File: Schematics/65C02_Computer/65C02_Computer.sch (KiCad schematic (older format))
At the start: 1 part

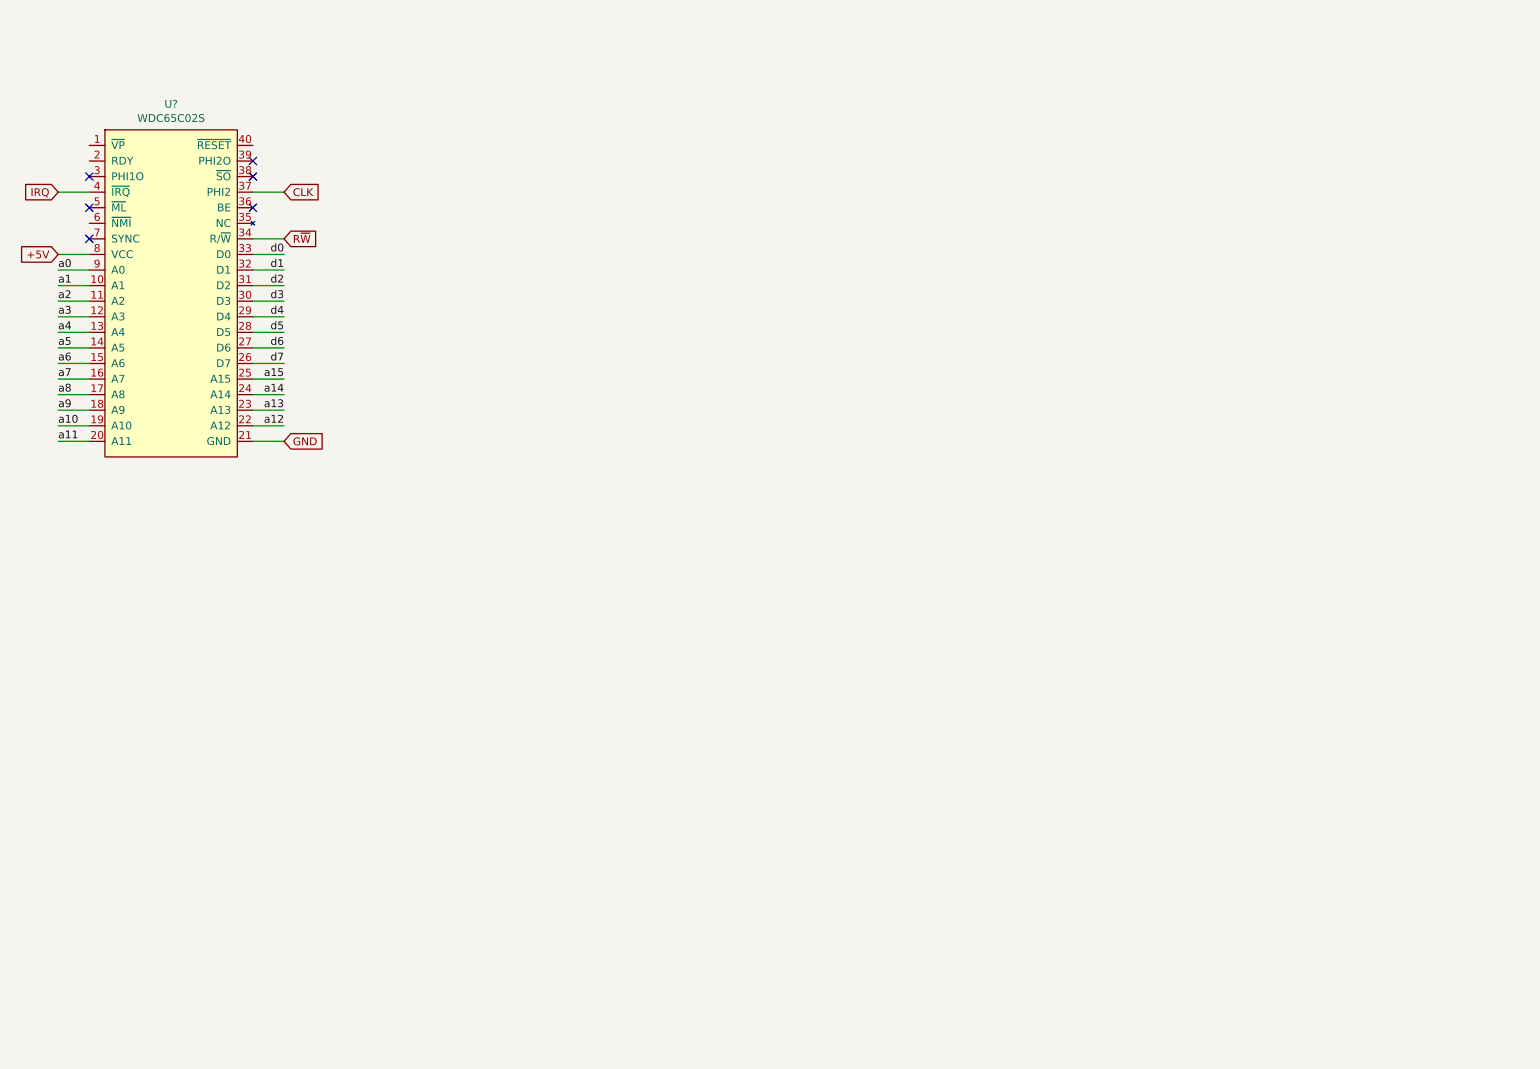
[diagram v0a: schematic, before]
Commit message: Added VIA chips to schematic
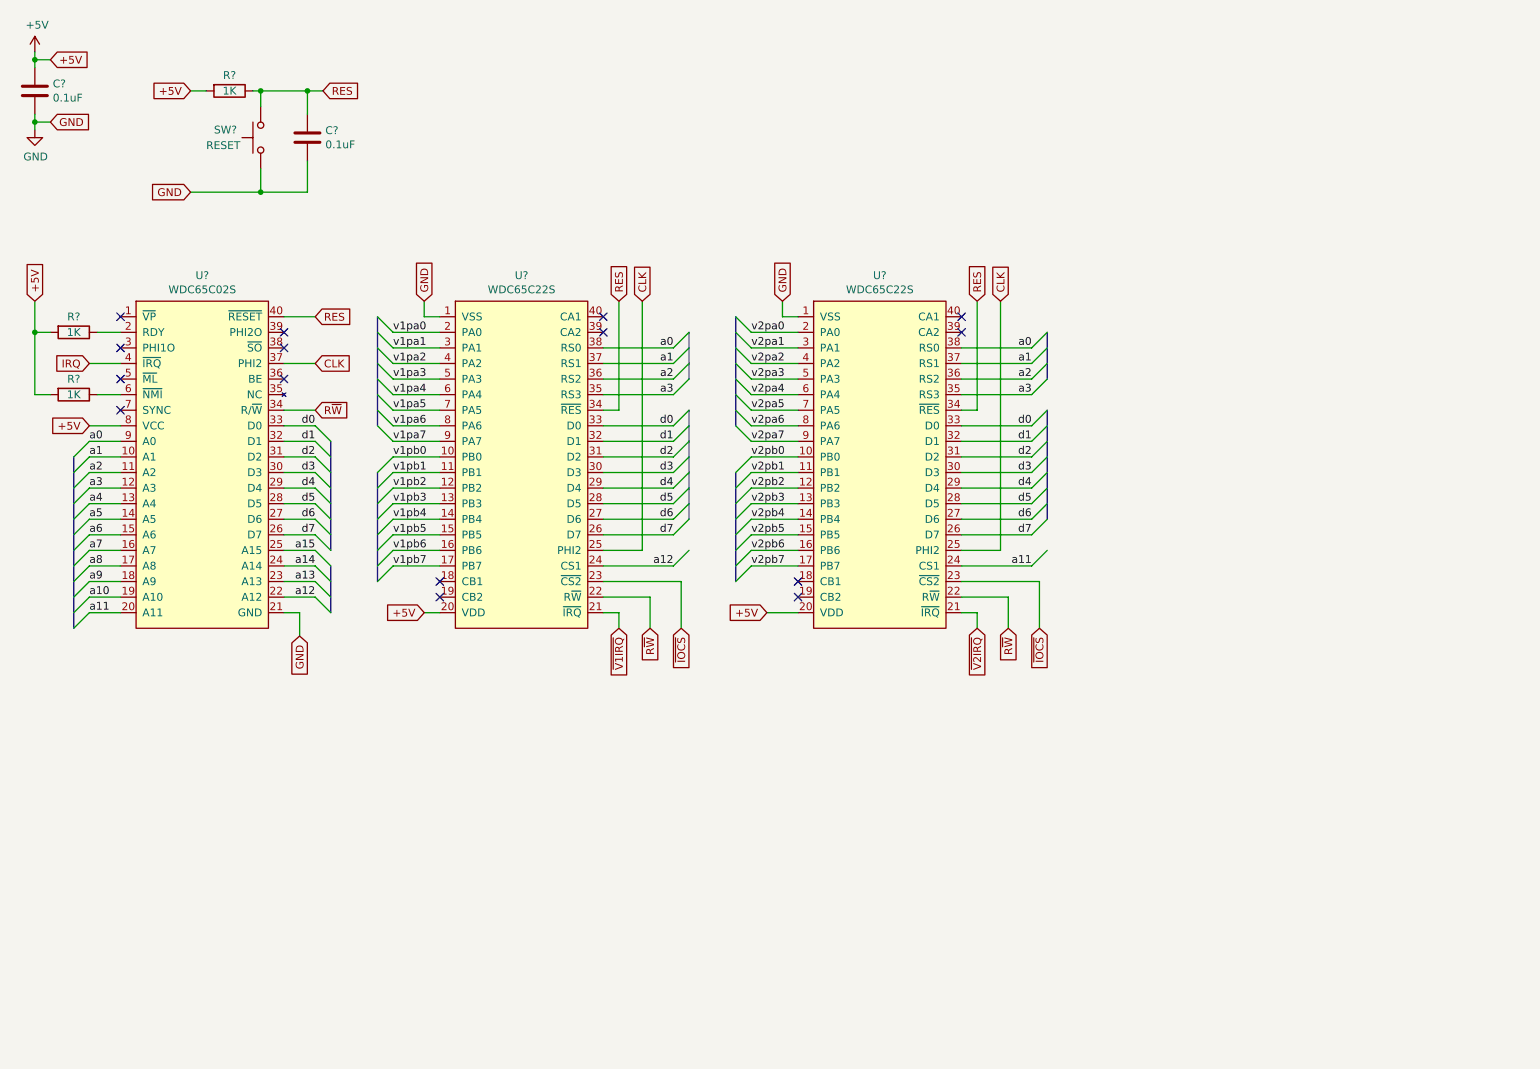
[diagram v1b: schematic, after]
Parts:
- added C? (x2): 0.1uF, symbol Device:C
- added R? (x3): 1K, symbol Device:R
- added SW?: RESET, symbol Switch:SW_Push
- added U? (x2): WDC65C22S, Package_DIP:DIP-40_W15.24mm_Socket, symbol 6502:WDC65C22S
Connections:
- net +5V: now also C?.1, R?.2, R?.2, R?.2, U?.20 (VDD), U?.20 (VDD)
- net CLK: now also U?.25 (PHI2), U?.25 (PHI2)
- net GND: now also C?.2, C?.2, SW?.1, U?.1 (VSS), U?.1 (VSS)
- net R~W: now also U?.22 (R~W), U?.22 (R~W)
- net a0: now also U?.38 (RS0), U?.38 (RS0)
- net a1: now also U?.37 (RS1), U?.37 (RS1)
- net a11: now also U?.24 (CS1)
- net a12: now also U?.24 (CS1)
- net a2: now also U?.36 (RS2), U?.36 (RS2)
- net a3: now also U?.35 (RS3), U?.35 (RS3)
- net d0: now also U?.33 (D0), U?.33 (D0)
- net d1: now also U?.32 (D1), U?.32 (D1)
- net d2: now also U?.31 (D2), U?.31 (D2)
- net d3: now also U?.30 (D3), U?.30 (D3)
- net d4: now also U?.29 (D4), U?.29 (D4)
- net d5: now also U?.28 (D5), U?.28 (D5)
- net d6: now also U?.27 (D6), U?.27 (D6)
- net d7: now also U?.26 (D7), U?.26 (D7)
- net at U?.2 (RDY): now also R?.1
- net RES: now reaches U?.40 (~RESET)
- net RES: now also C?.1, R?.1, SW?.2, U?.34 (~RES), U?.34 (~RES)
- net at U?.6 (~NMI): now also R?.1
- new net v1pa0: U?.2 (PA0)
- new net v1pa1: U?.3 (PA1)
- new net v1pa2: U?.4 (PA2)
- new net v1pa3: U?.5 (PA3)
- new net v1pa4: U?.6 (PA4)
- new net v1pa5: U?.7 (PA5)
- new net v1pa6: U?.8 (PA6)
- new net v1pa7: U?.9 (PA7)
- new net v1pb0: U?.10 (PB0)
- new net v1pb1: U?.11 (PB1)
- new net v1pb2: U?.12 (PB2)
- new net v1pb3: U?.13 (PB3)
- new net v1pb4: U?.14 (PB4)
- new net v1pb5: U?.15 (PB5)
- new net v1pb6: U?.16 (PB6)
- new net v1pb7: U?.17 (PB7)
- new net v2pa0: U?.2 (PA0)
- new net v2pa1: U?.3 (PA1)
- new net v2pa2: U?.4 (PA2)
- new net v2pa3: U?.5 (PA3)
- new net v2pa4: U?.6 (PA4)
- new net v2pa5: U?.7 (PA5)
- new net v2pa6: U?.8 (PA6)
- new net v2pa7: U?.9 (PA7)
- new net v2pb0: U?.10 (PB0)
- new net v2pb1: U?.11 (PB1)
- new net v2pb2: U?.12 (PB2)
- new net v2pb3: U?.13 (PB3)
- new net v2pb4: U?.14 (PB4)
- new net v2pb5: U?.15 (PB5)
- new net v2pb6: U?.16 (PB6)
- new net v2pb7: U?.17 (PB7)
- new net ~IOCS: U?.23 (~CS2), U?.23 (~CS2)
- new net ~V1IRQ: U?.21 (~IRQ)
- new net ~V2IRQ: U?.21 (~IRQ)
- no-connect marks 6 -> 15
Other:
- moved on the sheet: U?

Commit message: Added two oscillators
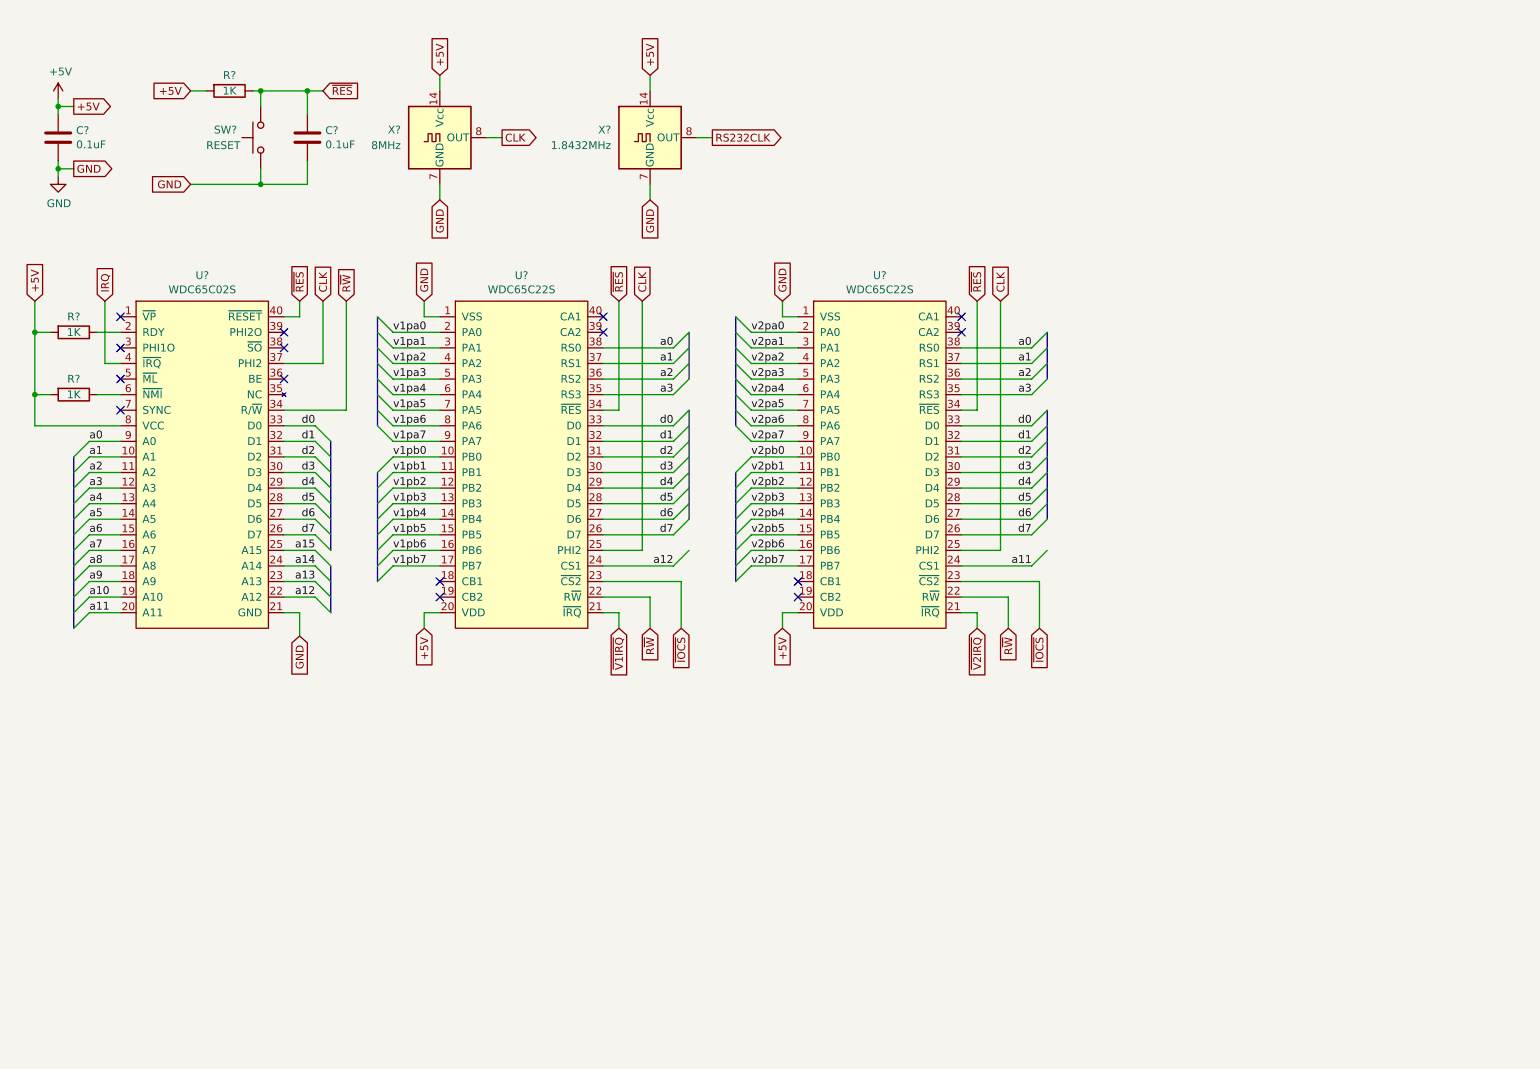
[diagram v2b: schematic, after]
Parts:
- added X?: 8MHz, Oscillator:Oscillator_DIP-14, symbol Oscillator:ACO-xxxMHz
- added X?: 1.8432MHz, Oscillator:Oscillator_DIP-14, symbol Oscillator:ACO-xxxMHz
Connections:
- net +5V: now also X?.14 (Vcc), X?.14 (Vcc)
- net CLK: now also X?.8 (OUT)
- net GND: now also X?.7 (GND), X?.7 (GND)
- net RES renamed ~RES
- new net RS232CLK: X?.8 (OUT)
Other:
- moved on the sheet: C?
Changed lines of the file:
@@
 encoding utf-8
 Sheet 1 1
-Title ""
-Date ""
-Rev ""
+Title "65C02 Hobby Computer"
+Date "2020-01-07"
+Rev "v001"
 Comp ""
 Comment1 ""
 Comment2 ""
-Comment3 ""
-Comment4 ""
+Comment3 "Based on Ben Eater's design"
+Comment4 "Author: Dawid Buchwald"
 $EndDescr
 $Comp
@@
 	1    0    0    -1
 $EndComp
-Text GLabel 1500 2900 0    50   Input ~ 0
+Text GLabel 1600 2500 1    50   Input ~ 0
 IRQ
 Wire Wire Line
-	1500 2900 1700 2900
-Text GLabel 2950 2900 2    50   Input ~ 0
+	1600 2500 1600 2900
+Text GLabel 3000 2500 1    50   Input ~ 0
 CLK
 Wire Wire Line
-	2950 2900 2750 2900
+	3000 2900 2750 2900
 Text GLabel 2850 4650 3    50   Input ~ 0
 GND
-Text GLabel 1500 3300 0    50   Input ~ 0
-+5V
-Wire Wire Line
-	1500 3300 1700 3300
 Text Label 1500 3400 0    50   ~ 0
 a0
@@
 Wire Wire Line
 	2750 3300 2950 3300
-Text GLabel 2950 3200 2    50   Input ~ 0
+Text GLabel 3150 2500 1    50   Input ~ 0
 R~W
 Wire Wire Line
-	2950 3200 2750 3200
+	3150 3200 2750 3200
 NoConn ~ 2750 3000
 NoConn ~ 2750 2800
@@
 Text GLabel 1150 2500 1    50   Input ~ 0
 +5V
-Text GLabel 2950 2600 2    50   Input ~ 0
-RES
-Wire Wire Line
-	2950 2600 2750 2600
+Text GLabel 2850 2500 1    50   Input ~ 0
+~RES
+Wire Wire Line
+	2850 2600 2750 2600
 Wire Wire Line
 	2750 4500 2850 4500
@@
 L power:+5V #PWR?
 U 1 1 5E15AAC6
-P 1150 900
-F 0 "#PWR?" H 1150 750 50  0001 C CNN
-F 1 "+5V" H 1165 1073 50  0000 C CNN
-F 2 "" H 1150 900 50  0001 C CNN
-F 3 "" H 1150 900 50  0001 C CNN
-	1    1150 900
+P 1300 1200
+F 0 "#PWR?" H 1300 1050 50  0001 C CNN
+F 1 "+5V" H 1315 1373 50  0000 C CNN
+F 2 "" H 1300 1200 50  0001 C CNN
+F 3 "" H 1300 1200 50  0001 C CNN
+	1    1300 1200
 	1    0    0    -1
 $EndComp
@@
 L power:GND #PWR?
 U 1 1 5E15AF3A
-P 1150 1400
-F 0 "#PWR?" H 1150 1150 50  0001 C CNN
-F 1 "GND" H 1155 1227 50  0000 C CNN
-F 2 "" H 1150 1400 50  0001 C CNN
-F 3 "" H 1150 1400 50  0001 C CNN
-	1    1150 1400
+P 1300 1700
+F 0 "#PWR?" H 1300 1450 50  0001 C CNN
+F 1 "GND" H 1305 1527 50  0000 C CNN
+F 2 "" H 1300 1700 50  0001 C CNN
+F 3 "" H 1300 1700 50  0001 C CNN
+	1    1300 1700
 	1    0    0    -1
 $EndComp
@@
 L Device:C C?
 U 1 1 5E15B54A
-P 1150 1150
-F 0 "C?" H 1265 1196 50  0000 L CNN
-F 1 "0.1uF" H 1265 1105 50  0000 L CNN
-F 2 "" H 1188 1000 50  0001 C CNN
-F 3 "~" H 1150 1150 50  0001 C CNN
-	1    1150 1150
+P 1300 1450
+F 0 "C?" H 1415 1496 50  0000 L CNN
+F 1 "0.1uF" H 1415 1405 50  0000 L CNN
+F 2 "" H 1338 1300 50  0001 C CNN
+F 3 "~" H 1300 1450 50  0001 C CNN
+	1    1300 1450
 	1    0    0    -1
 $EndComp
 Wire Wire Line
-	1150 900  1150 950
-Wire Wire Line
-	1150 1300 1150 1350
-Text GLabel 1250 950  2    50   Input ~ 0
+	1300 1200 1300 1250
+Wire Wire Line
+	1300 1600 1300 1650
+Text GLabel 1400 1250 2    50   Output ~ 0
 +5V
-Text GLabel 1250 1350 2    50   Input ~ 0
+Text GLabel 1400 1650 2    50   Output ~ 0
 GND
 Wire Wire Line
-	1150 1350 1250 1350
-Connection ~ 1150 1350
-Wire Wire Line
-	1150 1350 1150 1400
-Wire Wire Line
-	1150 950  1250 950
-Connection ~ 1150 950
-Wire Wire Line
-	1150 950  1150 1000
+	1300 1650 1400 1650
+Connection ~ 1300 1650
+Wire Wire Line
+	1300 1650 1300 1700
+Wire Wire Line
+	1300 1250 1400 1250
+Connection ~ 1300 1250
+Wire Wire Line
+	1300 1250 1300 1300
 $Comp
 L Device:R R?
@@
 	2150 1150 2250 1150
 Text GLabel 3000 1150 2    50   Input ~ 0
-RES
+~RES
 Wire Wire Line
 	2550 1150 2600 1150
@@
 	2900 1150 3000 1150
 Wire Wire Line
-	2600 1650 2600 1800
-Wire Wire Line
-	2600 1800 2900 1800
-Wire Wire Line
-	2900 1800 2900 1600
-Text GLabel 2150 1800 0    50   Input ~ 0
+	2600 1650 2600 1750
+Wire Wire Line
+	2600 1750 2900 1750
+Wire Wire Line
+	2900 1750 2900 1600
+Text GLabel 2150 1750 0    50   Input ~ 0
 GND
 Wire Wire Line
-	2150 1800 2600 1800
-Connection ~ 2600 1800
+	2150 1750 2600 1750
+Connection ~ 2600 1750
 $Comp
 L 6502:WDC65C22S U?
@@
 	1    0    0    -1
 $EndComp
-Text GLabel 3650 4500 0    50   Input ~ 0
+Text GLabel 3650 4600 3    50   Input ~ 0
 +5V
-Text GLabel 5850 4500 0    50   Input ~ 0
+Text GLabel 5950 4600 3    50   Input ~ 0
 +5V
 Wire Wire Line
-	5850 4500 6050 4500
+	5950 4500 6050 4500
 Text GLabel 4900 2500 1    50   Input ~ 0
-RES
+~RES
 Text GLabel 7200 2500 1    50   Input ~ 0
-RES
+~RES
 Wire Wire Line
 	4800 3200 4900 3200
@@
 Wire Wire Line
 	4800 4100 5050 4100
+Wire Wire Line
+	1150 3300 1150 3100
+Wire Wire Line
+	1150 3300 1700 3300
+Connection ~ 1150 3100
+Wire Wire Line
+	1600 2900 1700 2900
+Wire Wire Line
+	3150 3200 3150 2500
+Wire Wire Line
+	3000 2900 3000 2500
+Wire Wire Line
+	2850 2600 2850 2500
+$Comp
+L Oscillator:ACO-xxxMHz X?
+U 1 1 5E1CCFB4
+P 3750 1450
+F 0 "X?" H 3500 1500 50  0000 R CNN
+F 1 "8MHz" H 3500 1400 50  0000 R CNN
+F 2 "Oscillator:Oscillator_DIP-14" H 4200 1100 50  0001 C CNN
+F 3 "http://www.conwin.com/datasheets/cx/cx030.pdf" H 3650 1450 50  0001 C CNN
+	1    3750 1450
+	1    0    0    -1
+$EndComp
+Text GLabel 3750 1850 3    50   Input ~ 0
+GND
+Text GLabel 3750 1050 1    50   Input ~ 0
++5V
+Wire Wire Line
+	3750 1750 3750 1850
+Wire Wire Line
+	3750 1150 3750 1050
+Text GLabel 4150 1450 2    50   Output ~ 0
+CLK
+Wire Wire Line
+	4050 1450 4150 1450
+$Comp
+L Oscillator:ACO-xxxMHz X?
+U 1 1 5E1E750E
+P 5100 1450
+F 0 "X?" H 4850 1500 50  0000 R CNN
+F 1 "1.8432MHz" H 4850 1400 50  0000 R CNN
+F 2 "Oscillator:Oscillator_DIP-14" H 5550 1100 50  0001 C CNN
+F 3 "http://www.conwin.com/datasheets/cx/cx030.pdf" H 5000 1450 50  0001 C CNN
+	1    5100 1450
+	1    0    0    -1
+$EndComp
+Text GLabel 5100 1050 1    50   Input ~ 0
++5V
+Text GLabel 5100 1850 3    50   Input ~ 0
+GND
+Wire Wire Line
+	5100 1850 5100 1750
+Wire Wire Line
+	5100 1050 5100 1150
+Text GLabel 5500 1450 2    50   Output ~ 0
+RS232CLK
+Wire Wire Line
+	5400 1450 5500 1450
+Wire Wire Line
+	3650 4500 3650 4600
+Wire Wire Line
+	5950 4600 5950 4500
 Wire Bus Line
 	3050 4200 3050 4500
